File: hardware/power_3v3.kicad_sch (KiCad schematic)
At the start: 0 parts

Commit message: Kicad şema düzenlemesi yapıldı.
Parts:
- added C10: 4.7nf, symbol Device:C
- added C11: 120uf, symbol Device:C
- added C12: 0.1uf, symbol Device:C
- added C5: 2.2nf, symbol Device:C
- added C6, C9: 100pf, symbol Device:C
- added C7: 180uf, symbol Device:C
- added C8: 0.01uf, symbol Device:C
- added D4: 3A, symbol Device:D_Schottky
- added L2: 10uh, symbol Device:L
- added R6: 33K, symbol Device:R
- added U2: LM2655MTCX-3.3, MTC16_TEX, symbol drip-irrigation-sys-cc:LM2655MTCX-3.3
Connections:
- net PWR_SOURCE_VCC: now also C7.1, C8.1, U2.5 (VIN), U2.7 (AVIN)
- new net: C6.1, R6.1, U2.10 (COMP)
- new net: C5.1, R6.2
- new net: C12.1, D4.1 (K), L2.1, U2.2 (SW)
- new net: C12.2, U2.6 (VCB)
- new net: C10.1, U2.8 (SS)
- new net: C9.2, U2.11 (Ldelay)
- new net GND: C10.2, C11.2, C5.2, C6.2, C7.2, C8.2, C9.1, D4.2 (A), U2.13 (GND)
- new net VCC_3.3V: C11.1, L2.2, U2.9 (FB)

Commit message: Kicad şema düzenlemesi yapıldı.
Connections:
- net PWR_SOURCE_VCC renamed +12V
- net VCC_3.3V renamed +3V3
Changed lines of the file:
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@@
   (junction (at 128.27 90.17) (diameter 0) (color 0 0 0 0)
   )
+  (junction (at 147.32 90.17) (diameter 0) (color 0 0 0 0)
+  )
+  (junction (at 260.35 82.55) (diameter 0) (color 0 0 0 0)
+  )
+  (junction (at 191.77 82.55) (diameter 0) (color 0 0 0 0)
+  )
   (junction (at 121.92 78.74) (diameter 0) (color 0 0 0 0)
   )
-  (junction (at 147.32 90.17) (diameter 0) (color 0 0 0 0)
-  )
-  (junction (at 260.35 82.55) (diameter 0) (color 0 0 0 0)
-  )
-  (junction (at 191.77 82.55) (diameter 0) (color 0 0 0 0)
-  )
   (junction (at 260.35 62.23) (diameter 0) (color 0 0 0 0)
   )
@@
     (stroke (width 0) (type default))
   )
+  (wire (pts (xy 191.77 82.55) (xy 219.71 82.55))
+    (stroke (width 0) (type default))
+  )
   (wire (pts (xy 128.27 90.17) (xy 134.62 90.17))
     (stroke (width 0) (type default))
   )
-  (wire (pts (xy 44.45 39.37) (xy 44.45 78.74))
-    (stroke (width 0) (type default))
-  )
-  (wire (pts (xy 36.83 39.37) (xy 44.45 39.37))
-    (stroke (width 0) (type default))
-  )
   (wire (pts (xy 147.32 90.17) (xy 166.37 90.17))
     (stroke (width 0) (type default))
@@
     (stroke (width 0) (type default))
   )
-  (wire (pts (xy 212.09 116.84) (xy 212.09 82.55))
-    (stroke (width 0) (type default))
-  )
   (wire (pts (xy 138.43 53.34) (xy 138.43 90.17))
     (stroke (width 0) (type default))
   )
-  (wire (pts (xy 212.09 82.55) (xy 191.77 82.55))
-    (stroke (width 0) (type default))
-  )
   (wire (pts (xy 207.01 66.04) (xy 242.57 66.04))
     (stroke (width 0) (type default))
@@
     (stroke (width 0) (type default))
   )
-  (wire (pts (xy 274.32 116.84) (xy 212.09 116.84))
-    (stroke (width 0) (type default))
-  )
   (wire (pts (xy 134.62 66.04) (xy 134.62 60.96))
     (stroke (width 0) (type default))
@@
     (stroke (width 0) (type default))
   )
+  (wire (pts (xy 219.71 78.74) (xy 219.71 82.55))
+    (stroke (width 0) (type default))
+  )
   (wire (pts (xy 134.62 60.96) (xy 140.97 60.96))
     (stroke (width 0) (type default))
@@
     (stroke (width 0) (type default))
   )
-  (wire (pts (xy 44.45 78.74) (xy 121.92 78.74))
-    (stroke (width 0) (type default))
-  )
   (wire (pts (xy 139.7 78.74) (xy 147.32 78.74))
     (stroke (width 0) (type default))
@@
     (stroke (width 0) (type default))
   )
+  (wire (pts (xy 121.92 73.66) (xy 121.92 78.74))
+    (stroke (width 0) (type default))
+  )
   (wire (pts (xy 207.01 63.5) (xy 213.36 63.5))
     (stroke (width 0) (type default))
   )
-  (hierarchical_label "VCC_3.3V" (shape input) (at 274.32 116.84 0) (fields_autoplaced)
-    (effects (font (size 1.27 1.27)) (justify left))
-  )
-  (hierarchical_label "PWR_SOURCE_GND" (shape input) (at 36.83 43.18 180) (fields_autoplaced)
-    (effects (font (size 1.27 1.27)) (justify right))
-  )
-  (hierarchical_label "PWR_SOURCE_VCC" (shape output) (at 36.83 39.37 180) (fields_autoplaced)
-    (effects (font (size 1.27 1.27)) (justify right))
-  )
-  (hierarchical_label "GND_3.3V" (shape input) (at 274.32 120.65 0) (fields_autoplaced)
-    (effects (font (size 1.27 1.27)) (justify left))
-  )
   (symbol (lib_id "Device:C") (at 191.77 88.9 0) (unit 1)
     (in_bom yes) (on_board yes) (dnp no) (fields_autoplaced)
@@
         (path "/41708c1e-19b2-4374-83f2-108076d82b45/4f778b49-8d1a-4c8f-a914-ecde21a56ebf/d7bbddbd-4fdd-4dff-98ef-2df59093286c"
           (reference "C11") (unit 1)
-        )
-      )
-    )
-  )
-  (symbol (lib_id "power:GND") (at 36.83 43.18 90) (unit 1)
-    (in_bom yes) (on_board yes) (dnp no) (fields_autoplaced)
-    (property "Reference" "#PWR09" (at 43.18 43.18 0)
-      (effects (font (size 1.27 1.27)) hide)
-    )
-    (property "Value" "GND" (at 40.64 43.18 90)
-      (effects (font (size 1.27 1.27)) (justify right))
-    )
-    (property "Footprint" "" (at 36.83 43.18 0)
-      (effects (font (size 1.27 1.27)) hide)
-    )
-    (property "Datasheet" "" (at 36.83 43.18 0)
-      (effects (font (size 1.27 1.27)) hide)
-    )
-    (pin "1")
-    (instances
-      (project "drip-irrigation-sys-cc"
-        (path "/41708c1e-19b2-4374-83f2-108076d82b45/4f778b49-8d1a-4c8f-a914-ecde21a56ebf/d7bbddbd-4fdd-4dff-98ef-2df59093286c"
-          (reference "#PWR09") (unit 1)
-        )
-      )
-    )
-  )
-  (symbol (lib_id "power:GND") (at 274.32 120.65 270) (unit 1)
-    (in_bom yes) (on_board yes) (dnp no) (fields_autoplaced)
-    (property "Reference" "#PWR08" (at 267.97 120.65 0)
-      (effects (font (size 1.27 1.27)) hide)
-    )
-    (property "Value" "GND" (at 270.51 120.65 90)
-      (effects (font (size 1.27 1.27)) (justify right))
-    )
-    (property "Footprint" "" (at 274.32 120.65 0)
-      (effects (font (size 1.27 1.27)) hide)
-    )
-    (property "Datasheet" "" (at 274.32 120.65 0)
-      (effects (font (size 1.27 1.27)) hide)
-    )
-    (pin "1")
-    (instances
-      (project "drip-irrigation-sys-cc"
-        (path "/41708c1e-19b2-4374-83f2-108076d82b45/4f778b49-8d1a-4c8f-a914-ecde21a56ebf/d7bbddbd-4fdd-4dff-98ef-2df59093286c"
-          (reference "#PWR08") (unit 1)
         )
       )
@@
     )
   )
+  (symbol (lib_id "power:+12V") (at 121.92 73.66 0) (unit 1)
+    (in_bom yes) (on_board yes) (dnp no) (fields_autoplaced)
+    (property "Reference" "#PWR09" (at 121.92 77.47 0)
+      (effects (font (size 1.27 1.27)) hide)
+    )
+    (property "Value" "+12V" (at 121.92 68.58 0)
+      (effects (font (size 1.27 1.27)))
+    )
+    (property "Footprint" "" (at 121.92 73.66 0)
+      (effects (font (size 1.27 1.27)) hide)
+    )
+    (property "Datasheet" "" (at 121.92 73.66 0)
+      (effects (font (size 1.27 1.27)) hide)
+    )
+    (pin "1")
+    (instances
+      (project "drip-irrigation-sys-cc"
+        (path "/41708c1e-19b2-4374-83f2-108076d82b45/4f778b49-8d1a-4c8f-a914-ecde21a56ebf/d7bbddbd-4fdd-4dff-98ef-2df59093286c"
+          (reference "#PWR09") (unit 1)
+        )
+      )
+    )
+  )
   (symbol (lib_id "Device:C") (at 267.97 73.66 0) (unit 1)
     (in_bom yes) (on_board yes) (dnp no) (fields_autoplaced)
@@
         )
       )
+    )
+  )
+  (symbol (lib_id "power:+3V3") (at 219.71 78.74 0) (unit 1)
+    (in_bom yes) (on_board yes) (dnp no) (fields_autoplaced)
+    (property "Reference" "#PWR012" (at 219.71 82.55 0)
+      (effects (font (size 1.27 1.27)) hide)
+    )
+    (property "Value" "+3V3" (at 219.71 73.66 0)
+      (effects (font (size 1.27 1.27)))
+    )
+    (property "Footprint" "" (at 219.71 78.74 0)
+      (effects (font (size 1.27 1.27)) hide)
+    )
+    (property "Datasheet" "" (at 219.71 78.74 0)
+      (effects (font (size 1.27 1.27)) hide)
+    )
+    (pin "1")
+    (instances
+      (project "drip-irrigation-sys-cc"
+        (path "/41708c1e-19b2-4374-83f2-108076d82b45"
+          (reference "#PWR012") (unit 1)
+        )
+        (path "/41708c1e-19b2-4374-83f2-108076d82b45/4f778b49-8d1a-4c8f-a914-ecde21a56ebf"
+          (reference "#PWR012") (unit 1)
+        )
+        (path "/41708c1e-19b2-4374-83f2-108076d82b45/4f778b49-8d1a-4c8f-a914-ecde21a56ebf/d7bbddbd-4fdd-4dff-98ef-2df59093286c"
+          (reference "#PWR08") (unit 1)
+        )
+      )

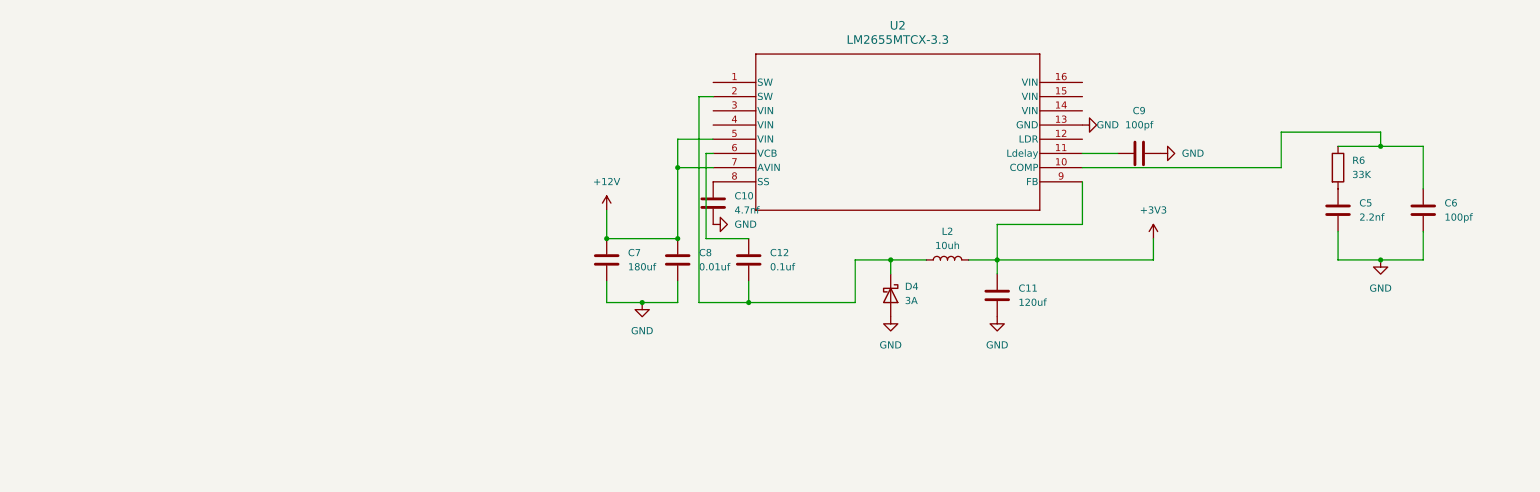
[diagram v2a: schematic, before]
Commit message: Kicad Power Modülü Tamamlandı.
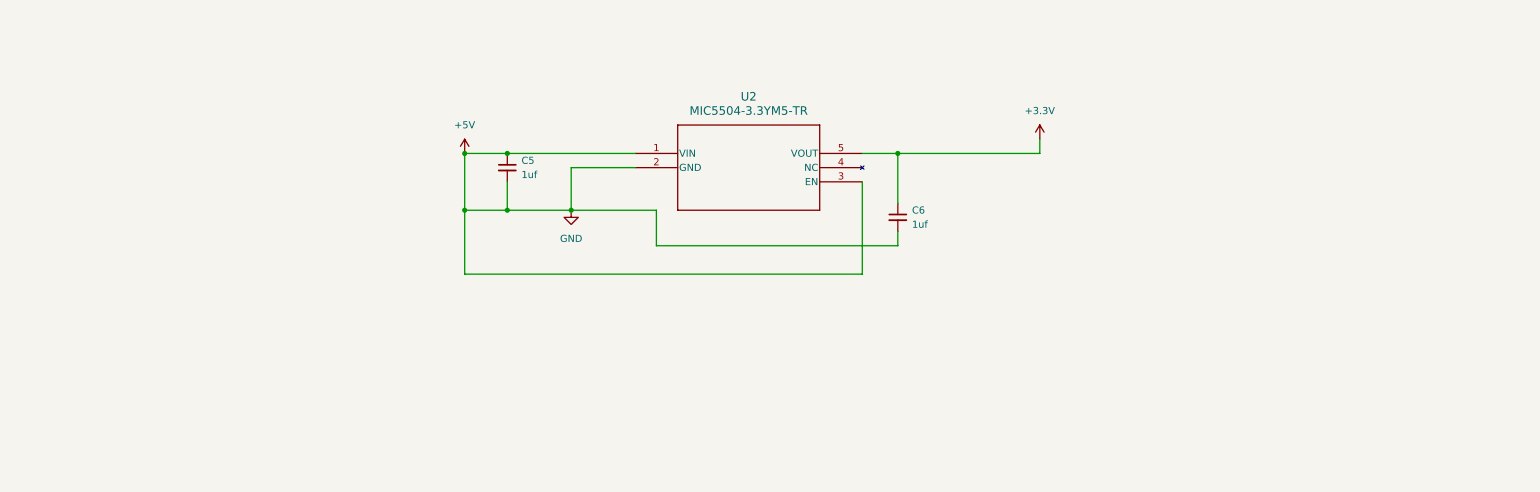
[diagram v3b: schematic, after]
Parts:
- removed C10: 4.7nf, symbol Device:C
- removed C11: 120uf, symbol Device:C
- removed C12: 0.1uf, symbol Device:C
- removed C5: 2.2nf, symbol Device:C
- removed C6, C9: 100pf, symbol Device:C
- removed C7: 180uf, symbol Device:C
- removed C8: 0.01uf, symbol Device:C
- removed D4: 3A, symbol Device:D_Schottky
- removed L2: 10uh, symbol Device:L
- removed R6: 33K, symbol Device:R
- removed U2: LM2655MTCX-3.3, MTC16_TEX, symbol drip-irrigation-sys-cc:LM2655MTCX-3.3
- added C5, C6: 1uf, symbol Device:C_Small
- added U2: MIC5504-3.3YM5-TR, drip-irrigation-sys-cc:MIC5504-3.3YM5-TR, symbol drip-irrigation-sys-cc:MIC5504-3.3YM5-TR
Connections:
- new net +3.3V: C6.1, U2.5 (VOUT)
- new net +5V: C5.1, C5.2, C6.2, U2.1 (VIN), U2.2 (GND), U2.3 (EN)

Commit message: Kicad şema düzenlemesi yapıldı.
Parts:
- C5, C6: footprint (none) -> Capacitor_SMD:C_0201_0603Metric; Digikey (none) -> 490-7229-2-ND
- U2: Digikey (none) -> MIC5504-3.3YM5-TR
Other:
- moved on the sheet: C5
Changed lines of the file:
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@@
+    (stroke (width 0) (type default))
+  )
+  (wire (pts (xy 104.14 66.04) (xy 104.14 63.5))
     (stroke (width 0) (type default))
   )
@@
     (stroke (width 0) (type default))
   )
-  (wire (pts (xy 104.14 73.66) (xy 104.14 68.58))
+  (wire (pts (xy 104.14 73.66) (xy 104.14 71.12))
     (stroke (width 0) (type default))
   )
@@
     (stroke (width 0) (type default))
   )
-  (symbol (lib_id "Device:C_Small") (at 104.14 66.04 0) (unit 1)
+  (symbol (lib_id "Device:C_Small") (at 104.14 68.58 0) (unit 1)
     (in_bom yes) (on_board yes) (dnp no) (fields_autoplaced)
-    (property "Reference" "C5" (at 106.68 64.7763 0)
+    (property "Reference" "C5" (at 106.68 67.3163 0)
       (effects (font (size 1.27 1.27)) (justify left))
     )
-    (property "Value" "1uf" (at 106.68 67.3163 0)
+    (property "Value" "1uf" (at 106.68 69.8563 0)
       (effects (font (size 1.27 1.27)) (justify left))
     )
-    (property "Footprint" "" (at 104.14 66.04 0)
+    (property "Footprint" "Capacitor_SMD:C_0201_0603Metric" (at 104.14 68.58 0)
       (effects (font (size 1.27 1.27)) hide)
     )
-    (property "Datasheet" "~" (at 104.14 66.04 0)
+    (property "Datasheet" "~" (at 104.14 68.58 0)
+      (effects (font (size 1.27 1.27)) hide)
+    )
+    (property "Digikey" "490-7229-2-ND" (at 104.14 68.58 0)
       (effects (font (size 1.27 1.27)) hide)
     )
@@
     (property "Datasheet" "MIC5504-3.3YM5-TR" (at 147.32 71.12 0)
       (effects (font (size 1.27 1.27) italic) hide)
+    )
+    (property "Digikey" "MIC5504-3.3YM5-TR" (at 127 63.5 0)
+      (effects (font (size 1.27 1.27)) hide)
     )
     (pin "1")
@@
       (effects (font (size 1.27 1.27)) (justify left))
     )
-    (property "Footprint" "" (at 173.99 74.93 0)
+    (property "Footprint" "Capacitor_SMD:C_0201_0603Metric" (at 173.99 74.93 0)
       (effects (font (size 1.27 1.27)) hide)
     )
@@
       (effects (font (size 1.27 1.27)) hide)
     )
+    (property "Digikey" "490-7229-2-ND" (at 173.99 74.93 0)
+      (effects (font (size 1.27 1.27)) hide)
+    )

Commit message: Kicad şema düzenlemesi yapıldı.
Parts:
- renumbered C5 to C24, C6 to C25, U2 to U4
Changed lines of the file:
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@@
   (symbol (lib_id "Device:C_Small") (at 104.14 68.58 0) (unit 1)
     (in_bom yes) (on_board yes) (dnp no) (fields_autoplaced)
-    (property "Reference" "C5" (at 106.68 67.3163 0)
+    (property "Reference" "C24" (at 106.68 67.3163 0)
       (effects (font (size 1.27 1.27)) (justify left))
     )
@@
       (project "drip-irrigation-sys-cc"
         (path "/41708c1e-19b2-4374-83f2-108076d82b45/4f778b49-8d1a-4c8f-a914-ecde21a56ebf/d7bbddbd-4fdd-4dff-98ef-2df59093286c"
-          (reference "C5") (unit 1)
+          (reference "C24") (unit 1)
         )
       )
@@
   (symbol (lib_id "drip-irrigation-sys-cc:MIC5504-3.3YM5-TR") (at 127 63.5 0) (unit 1)
     (in_bom yes) (on_board yes) (dnp no) (fields_autoplaced)
-    (property "Reference" "U2" (at 147.32 53.34 0)
+    (property "Reference" "U4" (at 147.32 53.34 0)
       (effects (font (size 1.524 1.524)))
     )
@@
       (project "drip-irrigation-sys-cc"
         (path "/41708c1e-19b2-4374-83f2-108076d82b45/4f778b49-8d1a-4c8f-a914-ecde21a56ebf/d7bbddbd-4fdd-4dff-98ef-2df59093286c"
-          (reference "U2") (unit 1)
+          (reference "U4") (unit 1)
         )
       )
@@
   (symbol (lib_id "power:+5V") (at 96.52 63.5 0) (unit 1)
     (in_bom yes) (on_board yes) (dnp no) (fields_autoplaced)
-    (property "Reference" "#PWR01" (at 96.52 67.31 0)
+    (property "Reference" "#PWR044" (at 96.52 67.31 0)
       (effects (font (size 1.27 1.27)) hide)
     )
@@
       (project "drip-irrigation-sys-cc"
         (path "/41708c1e-19b2-4374-83f2-108076d82b45/4f778b49-8d1a-4c8f-a914-ecde21a56ebf/d7bbddbd-4fdd-4dff-98ef-2df59093286c"
-          (reference "#PWR01") (unit 1)
+          (reference "#PWR044") (unit 1)
         )
       )
@@
   (symbol (lib_id "Device:C_Small") (at 173.99 74.93 0) (unit 1)
     (in_bom yes) (on_board yes) (dnp no) (fields_autoplaced)
-    (property "Reference" "C6" (at 176.53 73.6663 0)
+    (property "Reference" "C25" (at 176.53 73.6663 0)
       (effects (font (size 1.27 1.27)) (justify left))
     )
@@
       (project "drip-irrigation-sys-cc"
         (path "/41708c1e-19b2-4374-83f2-108076d82b45/4f778b49-8d1a-4c8f-a914-ecde21a56ebf/d7bbddbd-4fdd-4dff-98ef-2df59093286c"
-          (reference "C6") (unit 1)
+          (reference "C25") (unit 1)
         )
       )
@@
   (symbol (lib_id "power:GND") (at 115.57 73.66 0) (unit 1)
     (in_bom yes) (on_board yes) (dnp no) (fields_autoplaced)
-    (property "Reference" "#PWR02" (at 115.57 80.01 0)
+    (property "Reference" "#PWR045" (at 115.57 80.01 0)
       (effects (font (size 1.27 1.27)) hide)
     )
@@
       (project "drip-irrigation-sys-cc"
         (path "/41708c1e-19b2-4374-83f2-108076d82b45/4f778b49-8d1a-4c8f-a914-ecde21a56ebf/d7bbddbd-4fdd-4dff-98ef-2df59093286c"
-          (reference "#PWR02") (unit 1)
+          (reference "#PWR045") (unit 1)
         )
       )
@@
   (symbol (lib_id "power:+3.3V") (at 199.39 60.96 0) (unit 1)
     (in_bom yes) (on_board yes) (dnp no) (fields_autoplaced)
-    (property "Reference" "#PWR03" (at 199.39 64.77 0)
+    (property "Reference" "#PWR046" (at 199.39 64.77 0)
       (effects (font (size 1.27 1.27)) hide)
     )
@@
       (project "drip-irrigation-sys-cc"
         (path "/41708c1e-19b2-4374-83f2-108076d82b45/4f778b49-8d1a-4c8f-a914-ecde21a56ebf/d7bbddbd-4fdd-4dff-98ef-2df59093286c"
-          (reference "#PWR03") (unit 1)
+          (reference "#PWR046") (unit 1)
         )
       )

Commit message: PCB düzenlemesi yapıldı.
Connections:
- net +5V: no longer C24.2, C25.2, U4.2 (GND)
- new net GND: C24.2, C25.2, U4.2 (GND)
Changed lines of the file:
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@@
   (junction (at 104.14 63.5) (diameter 0) (color 0 0 0 0)
-  )
-  (junction (at 96.52 73.66) (diameter 0) (color 0 0 0 0)
-  )
-  (junction (at 104.14 73.66) (diameter 0) (color 0 0 0 0)
   )
   (wire (pts (xy 173.99 63.5) (xy 199.39 63.5))
@@
     (stroke (width 0) (type default))
   )
-  (wire (pts (xy 96.52 63.5) (xy 96.52 73.66))
+  (wire (pts (xy 96.52 63.5) (xy 96.52 85.09))
     (stroke (width 0) (type default))
   )
@@
     (stroke (width 0) (type default))
   )
-  (wire (pts (xy 96.52 73.66) (xy 104.14 73.66))
-    (stroke (width 0) (type default))
-  )
   (wire (pts (xy 115.57 66.04) (xy 115.57 73.66))
     (stroke (width 0) (type default))
@@
     (stroke (width 0) (type default))
   )
-  (wire (pts (xy 96.52 73.66) (xy 96.52 85.09))
-    (stroke (width 0) (type default))
-  )
